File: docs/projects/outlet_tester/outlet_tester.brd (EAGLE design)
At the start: 100 x 80 mm, 20 parts

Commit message: fix airwires
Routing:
- net 1: track 0.00 -> 49.5 mm
- net GND: track 0.00 -> 44.2 mm
- net 2: track 0.00 -> 28.9 mm
- net N$8: track 0.00 -> 23.5 mm
- net N$13: track 0.00 -> 23.2 mm
- net N$3: track 0.00 -> 22.4 mm
- net N$12: track 0.00 -> 21.9 mm
- net N$7: track 0.00 -> 18.2 mm
- net N$2: track 0.00 -> 16.8 mm
- net N$5: track 0.00 -> 15.2 mm
- net N$1: track 0.00 -> 13.5 mm
- net N$4: track 0.00 -> 8.15 mm
- net N$6: track 0.00 -> 6.88 mm
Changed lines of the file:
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@@
 <contactref element="D2" pad="C"/>
 <contactref element="D1" pad="C"/>
-<wire x1="13.97" y1="26.67" x2="7.62" y2="26.67" width="0" layer="19" extent="1-1"/>
-<wire x1="22.86" y1="22.86" x2="13.97" y2="26.67" width="0" layer="19" extent="1-1"/>
+<wire x1="13.97" y1="26.67" x2="7.62" y2="26.67" width="0.254" layer="1"/>
+<wire x1="19.05" y1="26.67" x2="22.86" y2="22.86" width="0.254" layer="16"/>
+<wire x1="13.97" y1="26.67" x2="19.05" y2="26.67" width="0.254" layer="16"/>
 </signal>
 <signal name="N$3">
@@
 <contactref element="R1" pad="2"/>
 <contactref element="D2" pad="A"/>
-<wire x1="13.97" y1="16.51" x2="22.86" y2="20.32" width="0" layer="19" extent="1-1"/>
-<wire x1="24.13" y1="8.89" x2="22.86" y2="20.32" width="0" layer="19" extent="1-1"/>
+<wire x1="17.78" y1="20.32" x2="13.97" y2="16.51" width="0.254" layer="16"/>
+<wire x1="22.86" y1="20.32" x2="17.78" y2="20.32" width="0.254" layer="16"/>
+<wire x1="22.86" y1="10.16" x2="24.13" y2="8.89" width="0.254" layer="1"/>
+<wire x1="22.86" y1="20.32" x2="22.86" y2="10.16" width="0.254" layer="1"/>
 </signal>
 <signal name="GND">
@@
 <contactref element="GND" pad="TP"/>
 <contactref element="S1" pad="4"/>
-<wire x1="49.53" y1="6.35" x2="66.04" y2="8.89" width="0" layer="19" extent="1-1"/>
-<wire x1="34.29" y1="8.89" x2="49.53" y2="6.35" width="0" layer="19" extent="1-1"/>
-<wire x1="40.64" y1="20.32" x2="34.29" y2="8.89" width="0" layer="19" extent="1-1"/>
+<wire x1="40.64" y1="15.24" x2="34.29" y2="8.89" width="0.254" layer="1"/>
+<wire x1="40.64" y1="20.32" x2="40.64" y2="15.24" width="0.254" layer="1"/>
+<wire x1="63.5" y1="6.35" x2="66.04" y2="8.89" width="0.254" layer="16"/>
+<wire x1="49.53" y1="6.35" x2="63.5" y2="6.35" width="0.254" layer="16"/>
+<wire x1="49.53" y1="6.35" x2="40.64" y2="15.24" width="0.254" layer="1"/>
 </signal>
 <signal name="1">
@@
 <contactref element="1" pad="TP"/>
 <contactref element="R7" pad="2"/>
-<wire x1="15.24" y1="60.96" x2="30.48" y2="74.93" width="0" layer="19" extent="1-1"/>
-<wire x1="15.24" y1="48.26" x2="15.24" y2="60.96" width="0" layer="19" extent="1-1"/>
-<wire x1="30.48" y1="46.99" x2="15.24" y2="48.26" width="0" layer="19" extent="1-1"/>
+<wire x1="15.24" y1="60.96" x2="15.24" y2="48.26" width="0.254" layer="1"/>
+<wire x1="29.21" y1="48.26" x2="30.48" y2="46.99" width="0.254" layer="16"/>
+<wire x1="15.24" y1="48.26" x2="29.21" y2="48.26" width="0.254" layer="16"/>
+<wire x1="16.51" y1="60.96" x2="30.48" y2="74.93" width="0.254" layer="16"/>
+<wire x1="15.24" y1="60.96" x2="16.51" y2="60.96" width="0.254" layer="16"/>
 </signal>
 <signal name="N$7">
@@
 <contactref element="D4" pad="C"/>
 <contactref element="D3" pad="C"/>
-<wire x1="83.82" y1="22.86" x2="92.71" y2="27.94" width="0" layer="19" extent="1-1"/>
-<wire x1="78.74" y1="27.94" x2="92.71" y2="27.94" width="0" layer="19" extent="1-1"/>
+<wire x1="78.74" y1="27.94" x2="83.82" y2="22.86" width="0.254" layer="1"/>
+<wire x1="87.63" y1="22.86" x2="92.71" y2="27.94" width="0.254" layer="16"/>
+<wire x1="83.82" y1="22.86" x2="87.63" y2="22.86" width="0.254" layer="16"/>
 </signal>
 <signal name="N$8">
@@
 <contactref element="R4" pad="2"/>
 <contactref element="D4" pad="A"/>
-<wire x1="83.82" y1="20.32" x2="92.71" y2="17.78" width="0" layer="19" extent="1-1"/>
-<wire x1="76.2" y1="8.89" x2="83.82" y2="20.32" width="0" layer="19" extent="1-1"/>
+<wire x1="83.82" y1="16.51" x2="76.2" y2="8.89" width="0.254" layer="1"/>
+<wire x1="83.82" y1="20.32" x2="83.82" y2="17.78" width="0.254" layer="1"/>
+<wire x1="83.82" y1="17.78" x2="83.82" y2="16.51" width="0.254" layer="1"/>
+<wire x1="83.82" y1="17.78" x2="92.71" y2="17.78" width="0.254" layer="1"/>
 </signal>
 <signal name="2">
@@
 <contactref element="2" pad="TP"/>
 <contactref element="R2" pad="1"/>
-<wire x1="76.2" y1="58.42" x2="86.36" y2="62.23" width="0" layer="19" extent="1-1"/>
-<wire x1="93.98" y1="48.26" x2="86.36" y2="62.23" width="0" layer="19" extent="1-1"/>
+<wire x1="80.01" y1="62.23" x2="76.2" y2="58.42" width="0.254" layer="16"/>
+<wire x1="86.36" y1="62.23" x2="80.01" y2="62.23" width="0.254" layer="16"/>
+<wire x1="86.36" y1="55.88" x2="93.98" y2="48.26" width="0.254" layer="1"/>
+<wire x1="86.36" y1="62.23" x2="86.36" y2="55.88" width="0.254" layer="1"/>
 </signal>
 <signal name="N$12">
@@
 <contactref element="D6" pad="C"/>
 <contactref element="D5" pad="C"/>
-<wire x1="46.99" y1="49.53" x2="50.8" y2="58.42" width="0" layer="19" extent="1-1"/>
-<wire x1="39.37" y1="58.42" x2="50.8" y2="58.42" width="0" layer="19" extent="1-1"/>
+<wire x1="50.8" y1="53.34" x2="46.99" y2="49.53" width="0.254" layer="1"/>
+<wire x1="50.8" y1="58.42" x2="50.8" y2="53.34" width="0.254" layer="1"/>
+<wire x1="50.8" y1="58.42" x2="39.37" y2="58.42" width="0.254" layer="1"/>
 </signal>
 <signal name="N$13">
@@
 <contactref element="R6" pad="2"/>
 <contactref element="D6" pad="A"/>
-<wire x1="57.15" y1="49.53" x2="66.04" y2="58.42" width="0" layer="19" extent="1-1"/>
-<wire x1="53.34" y1="58.42" x2="57.15" y2="49.53" width="0" layer="19" extent="1-1"/>
+<wire x1="53.34" y1="53.34" x2="57.15" y2="49.53" width="0.254" layer="1"/>
+<wire x1="53.34" y1="58.42" x2="53.34" y2="53.34" width="0.254" layer="1"/>
+<wire x1="53.34" y1="58.42" x2="66.04" y2="58.42" width="0.254" layer="1"/>
 </signal>
 <signal name="N$4">
 <contactref element="R3" pad="2"/>
 <contactref element="D1" pad="A"/>
-<wire x1="15.24" y1="38.1" x2="7.62" y2="36.83" width="0" layer="19" extent="1-1"/>
+<wire x1="8.89" y1="38.1" x2="7.62" y2="36.83" width="0.254" layer="16"/>
+<wire x1="15.24" y1="38.1" x2="8.89" y2="38.1" width="0.254" layer="16"/>
 </signal>
 <signal name="N$5">
 <contactref element="R2" pad="2"/>
 <contactref element="D3" pad="A"/>
-<wire x1="93.98" y1="38.1" x2="78.74" y2="38.1" width="0" layer="19" extent="1-1"/>
+<wire x1="93.98" y1="38.1" x2="78.74" y2="38.1" width="0.254" layer="1"/>
 </signal>
 <signal name="N$6">
 <contactref element="R5" pad="2"/>
 <contactref element="D5" pad="A"/>
-<wire x1="39.37" y1="68.58" x2="40.64" y2="74.93" width="0" layer="19" extent="1-1"/>
+<wire x1="40.64" y1="69.85" x2="39.37" y2="68.58" width="0.254" layer="1"/>
+<wire x1="40.64" y1="74.93" x2="40.64" y2="69.85" width="0.254" layer="1"/>
 </signal>
 <signal name="N$1">
 <contactref element="S1" pad="2"/>
 <contactref element="R7" pad="1"/>
-<wire x1="35.56" y1="25.4" x2="30.48" y2="36.83" width="0" layer="19" extent="1-1"/>
+<wire x1="35.56" y1="31.75" x2="30.48" y2="36.83" width="0.254" layer="1"/>
+<wire x1="35.56" y1="25.4" x2="35.56" y2="31.75" width="0.254" layer="1"/>
 </signal>
 </signals>

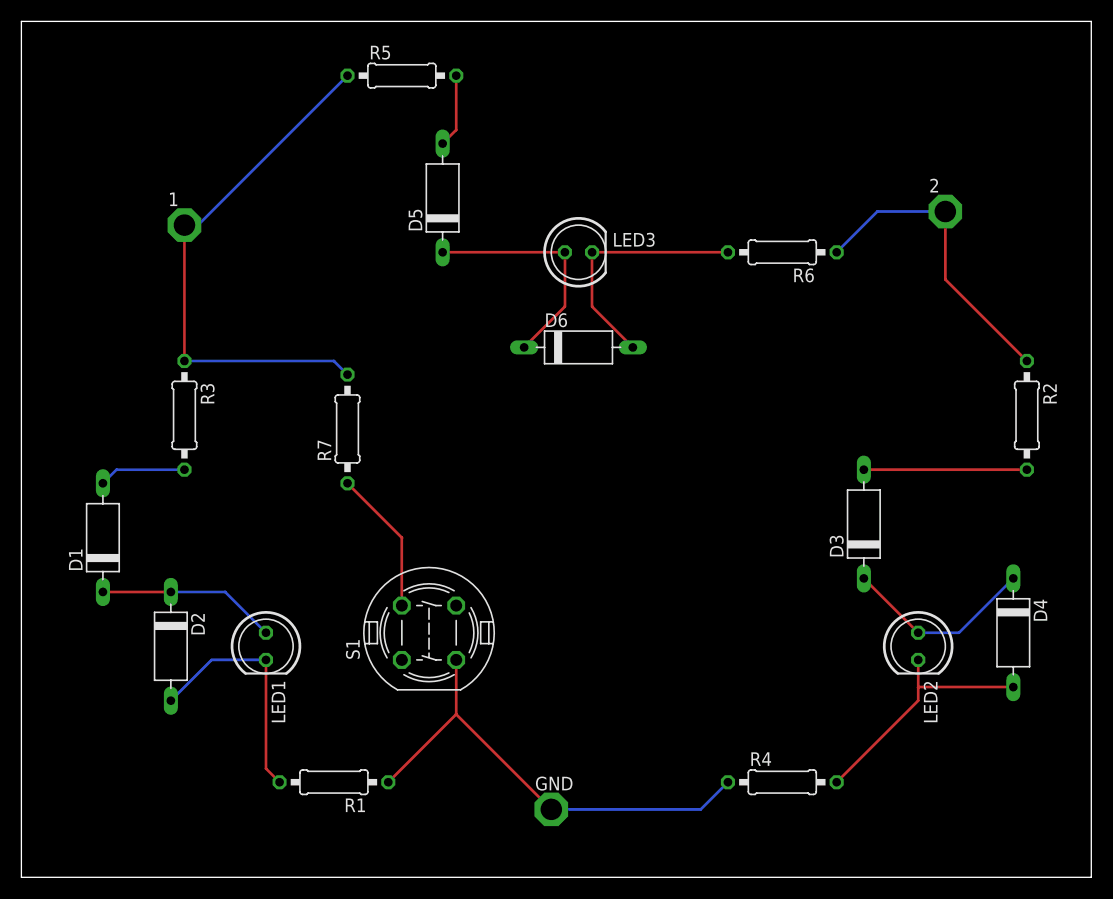
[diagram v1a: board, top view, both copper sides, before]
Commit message: outlet tester: adjust to available parts
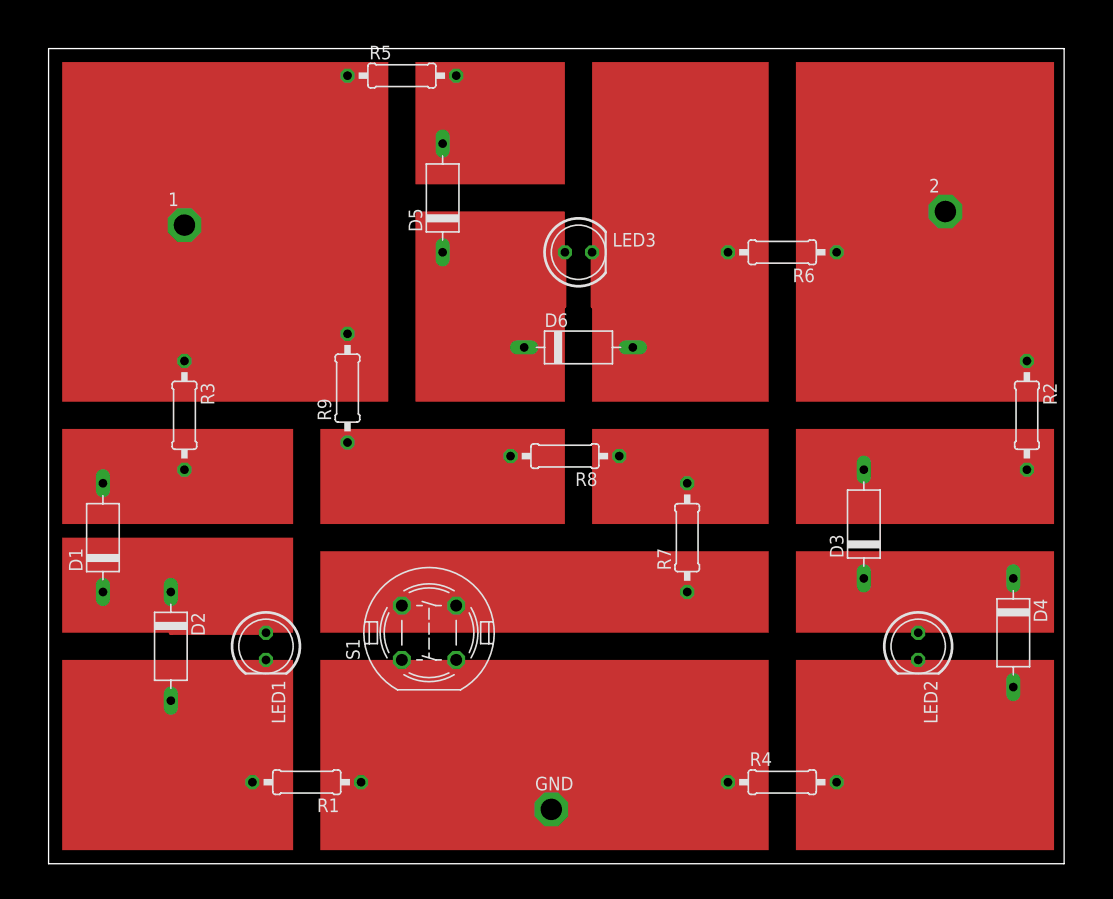
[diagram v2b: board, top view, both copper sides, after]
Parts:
- added R8, R9: 2.2k 3W, rcl:0207/10
- R7: value 6.8k 8W -> 2.2k 3W
- moved R7 33.3 mm to (62.2, 31.8)
- moved R1 2.54 mm to (26.7, 8.89)
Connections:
- new net N$10: R8.2, R9.1
- new net N$9: R7.2, R8.1
- net 1: now also R9.2; no longer R7.2
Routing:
- net N$10: track 0.00 -> 15.3 mm
- net N$1: track 13.5 -> 27.5 mm
- net N$9: track 0.00 -> 6.84 mm
- net GND: track 44.2 -> 50.9 mm
- net N$2: track 16.8 -> 19.1 mm
- net N$3: track 22.4 -> 20.6 mm
- net 2: track 28.9 -> 28.3 mm
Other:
- board size 100 x 80 mm -> 94.9 x 76.2 mm
